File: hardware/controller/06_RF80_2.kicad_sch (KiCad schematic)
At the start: 13 parts, among them U43 TCA9517DR

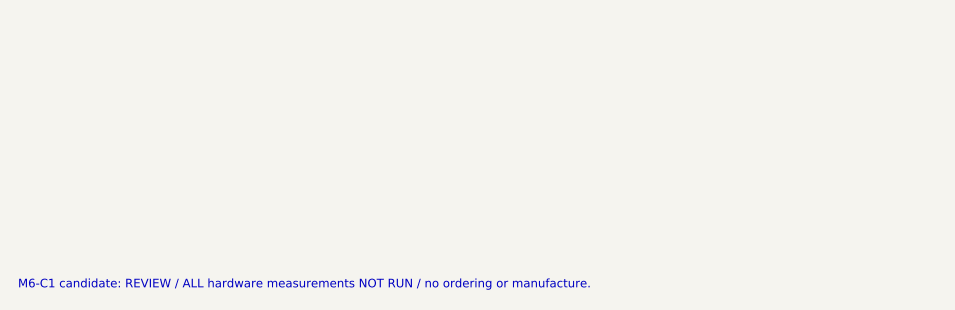
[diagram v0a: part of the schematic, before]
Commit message: M6-C1R1: protect pack identity input and review USB ESD topology
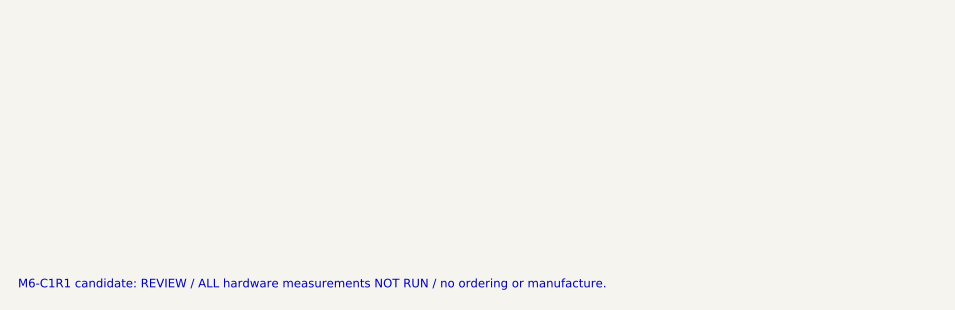
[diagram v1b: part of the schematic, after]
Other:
- note added: "M6-C1R1 candidate: REVIEW / ALL hardware measurements NOT RUN / no ordering or manufacture."
- note removed: "M6-C1 candidate: REVIEW / ALL hardware measurements NOT RUN / no ordering or manufacture."
